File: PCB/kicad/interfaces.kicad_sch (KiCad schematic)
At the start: 32 parts, among them IC9 534998-4, J1 1935174, J2 1935174, J3 826629-4, J7 Conn_01x01, J8 Conn_01x01, J9 USB_C_Receptacle_USB2.0

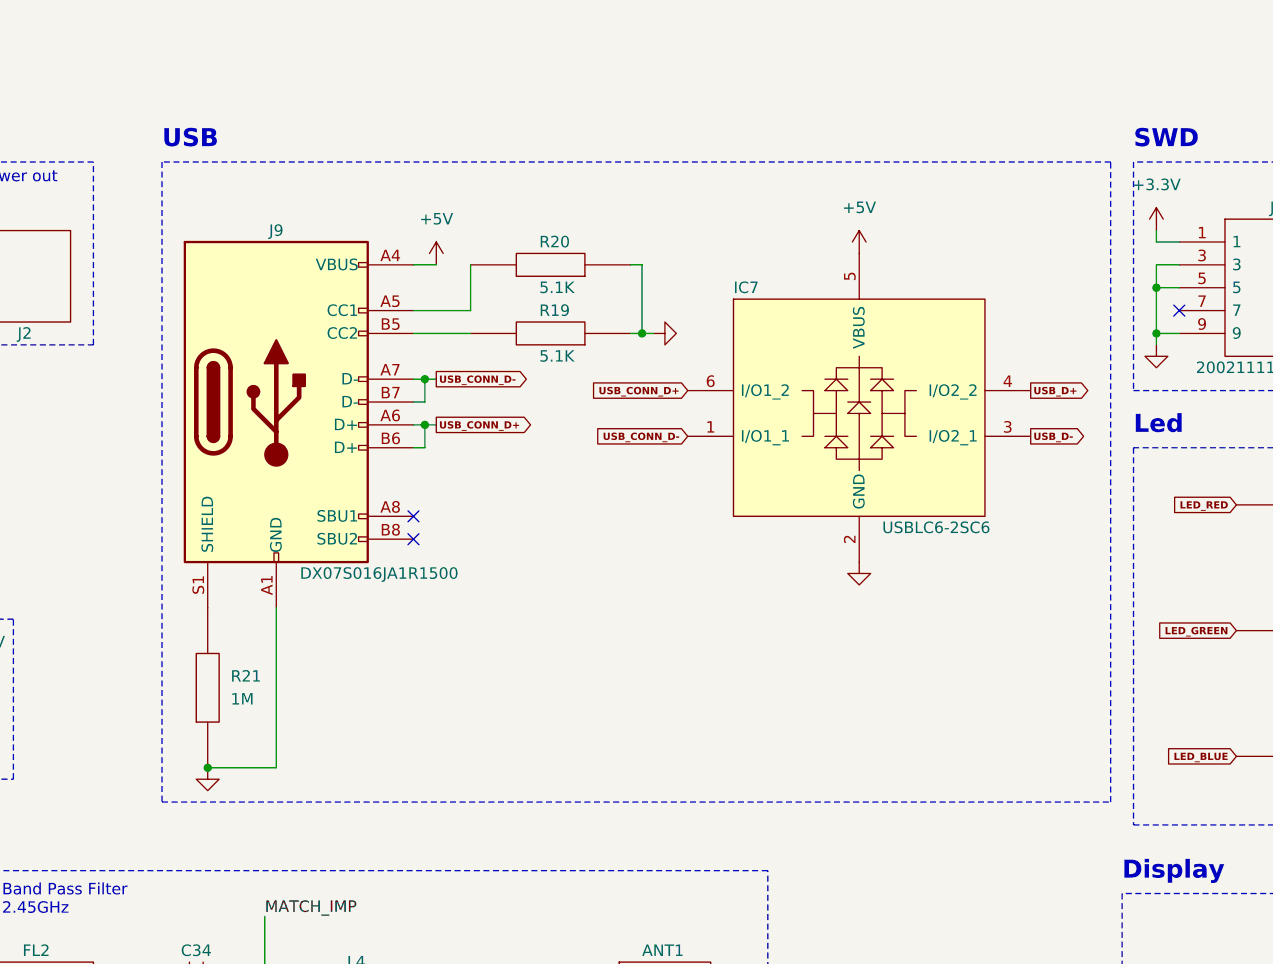
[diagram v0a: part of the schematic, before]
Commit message: PCB 1.0: - Corrected 5V generation - Corrected USB ESD protection - Replaced USB type-C with micro type-B
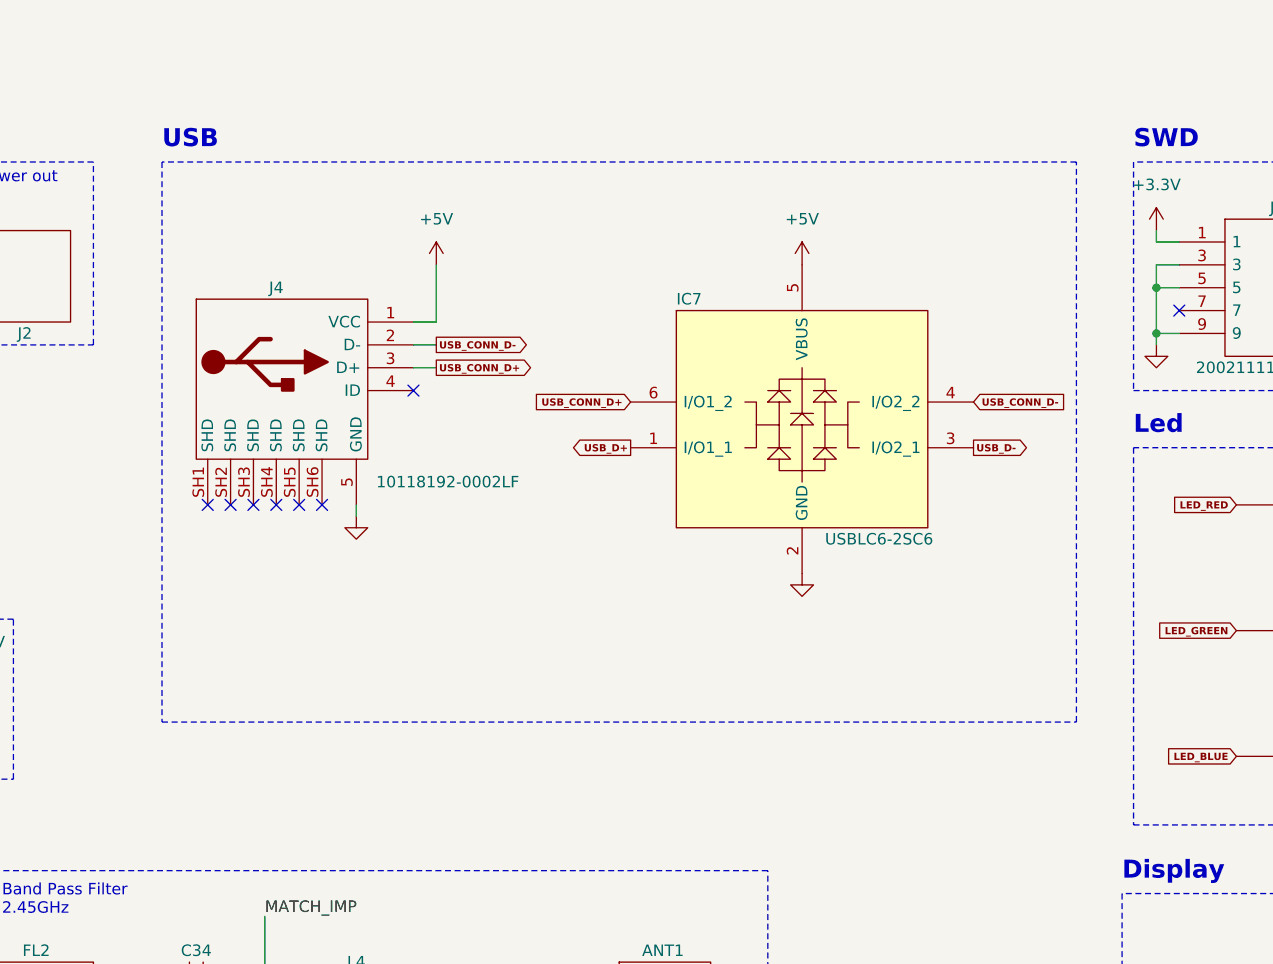
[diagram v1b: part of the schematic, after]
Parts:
- removed J9: USB_C_Receptacle_USB2.0, Connector_USB:USB_C_Receptacle_JAE_DX07S016JA1R1500, symbol Connector:USB_C_Receptacle_USB2.0
- removed R19, R20: 5.1K, alecot:RESC1608X55N, symbol alecot:ERJ-3EKF5101V
- removed R21: 1M, alecot:RESC1608X55N, symbol alecot:ERJ-3EKF1004V
- added J4: 10118192-0002LF, 101181920002LF, symbol alecot:10118192-0002LF
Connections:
- net +5V: now also J4.1 (VCC)
- net GND: now also J4.5 (GND)
- net USB_CONN_D+: now also J4.3 (D+)
- net USB_CONN_D-: now also IC7.4 (I/O2_2), J4.2 (D-); no longer IC7.1 (I/O1_1)
- net USB_D+: now also IC7.1 (I/O1_1); no longer IC7.4 (I/O2_2)
- no-connect marks 10 -> 15
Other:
- moved on the sheet: IC7

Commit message: Antenna chip replaced with antenna trace on PCB Switch replaced with button Added GND test point Added PD res on Boot pin Added NRST capacitor
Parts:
- removed ANT1: ANT3216LL00R2400A, alecot:ANT3216LL00R2400A, symbol alecot:ANT3216LL00R2400A
- removed C30: n.f., alecot:CAPC1005X55N, symbol alecot:GRM1555C1HR80BA01D
- removed L4: 0L, alecot:LQG15WH0N7B02D, symbol alecot:LQG15HS2N7S02D
- removed S1: PCM12SMTR, alecot:PCM12SMTR, symbol alecot:PCM12SMTR
- added C35: 1.2p, CAPC1005X55N, symbol alecot:GRM1555C1H1R2WA01D
- added L5: 3.6n, LQG15WH0N7B02D, symbol alecot:LQG15HS3N6S02D
- added R15: 10K, alecot:RESC1608X55N, symbol alecot:ERJ-3EKF1002V
- added S1: 800SP9B5M6RE, 800SP9B5M6RE, symbol alecot:800SP9B5M6RE
- added TP1: 5023, 5023, symbol alecot:5023
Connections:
- net +3.3V: now also S1.3
- net FEED: now also C35.2, L5.2
- net GND: now also C35.1, R15.1, S1.2, S1.4, TP1.1
- net MATCH_IMP: now also L5.1
- net SW_SWITCH: now also R15.2, S1.1
- no-connect marks 15 -> 10
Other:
- note added: "Button"
- note added: "Test Points"
- note removed: "Switch"
- moved on the sheet: C29, C3, C30, C34, FL2, H1, H2, H3, IC7, IC9, J1, J10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

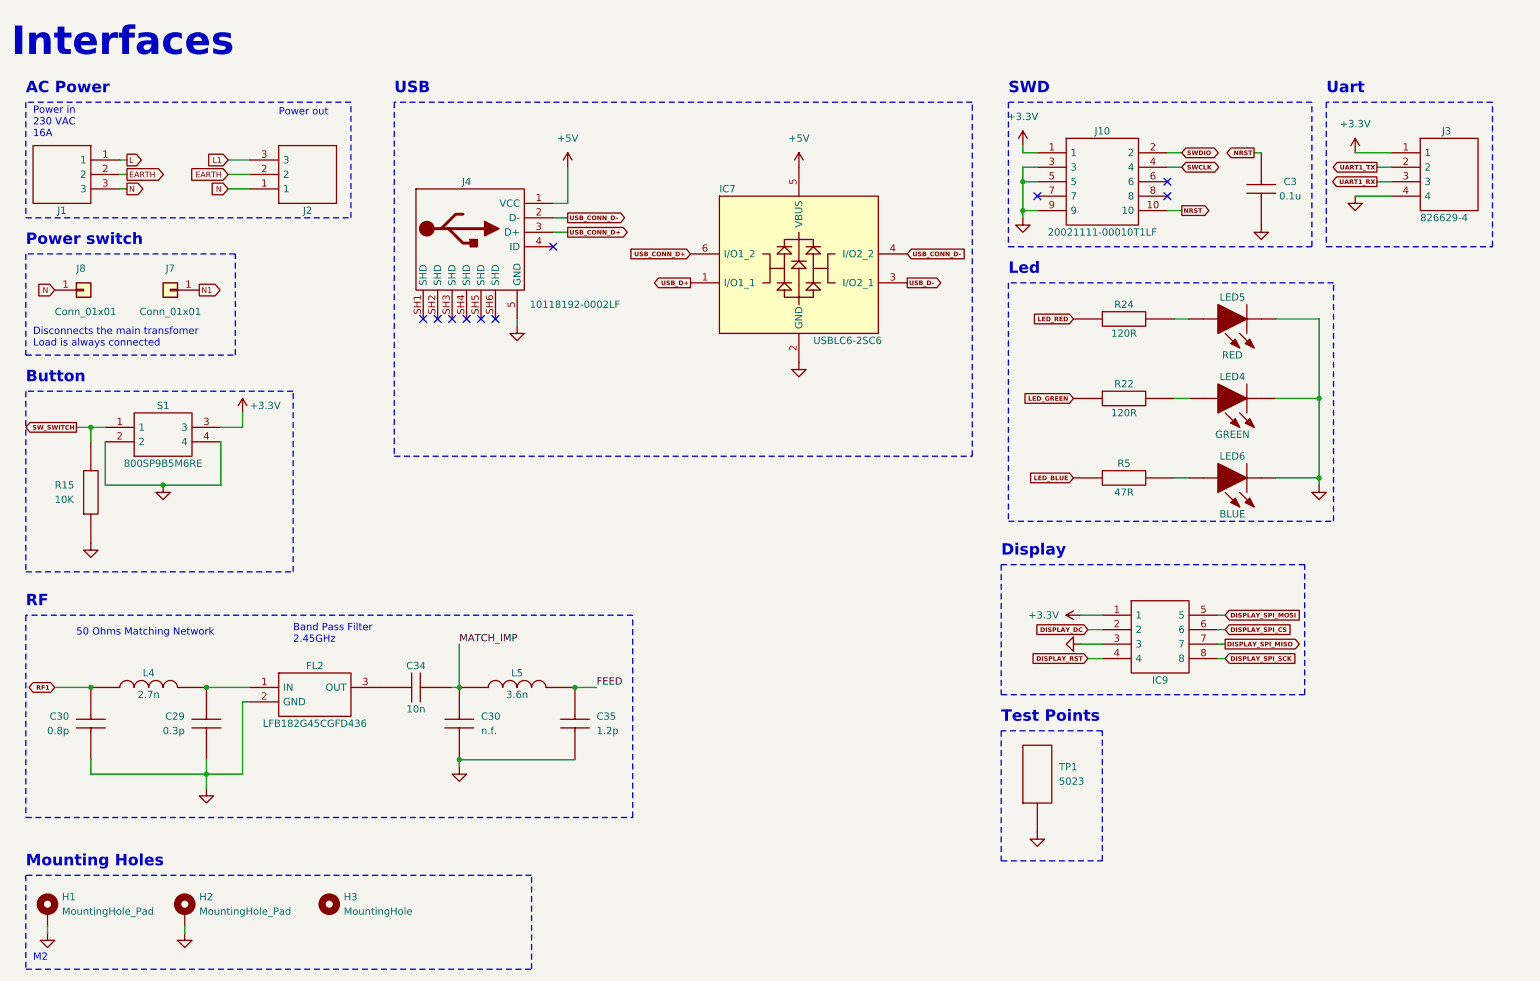
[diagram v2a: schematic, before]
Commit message: Added some test points
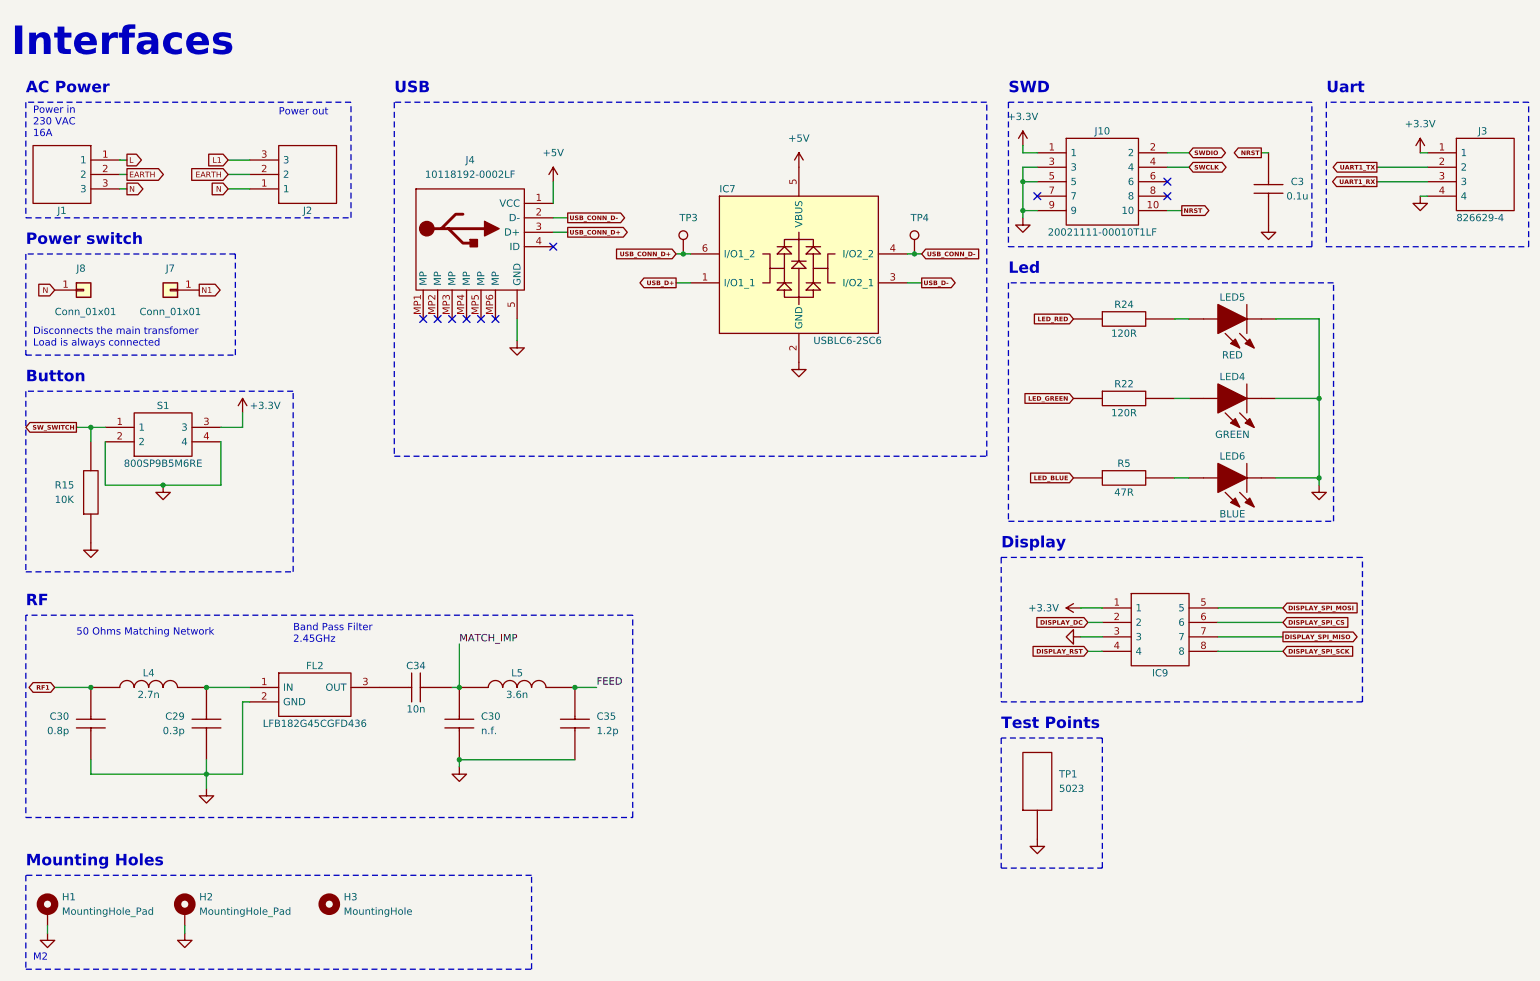
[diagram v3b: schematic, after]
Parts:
- added TP3, TP4: TestPoint, TestPoint:TestPoint_Pad_D1.0mm, symbol Connector:TestPoint
- C35: footprint CAPC1005X55N -> alecot:CAPC1005X55N
- L5: footprint LQG15WH0N7B02D -> alecot:LQG15WH0N7B02D
- S1: footprint 800SP9B5M6RE -> alecot:800SP9B5M6RE
- TP1: footprint 5023 -> alecot:5023
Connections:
- net USB_CONN_D+: now also TP3.1
- net USB_CONN_D-: now also TP4.1
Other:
- moved on the sheet: C3, IC9, J3, TP1
